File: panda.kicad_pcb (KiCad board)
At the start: 2 copper layers, 144.8 x 38.1 mm, 34 parts, among them J1 USB, J2 ICSP, U1 ATMEGA328-P, U2 MAX7219, Y1 12MHz

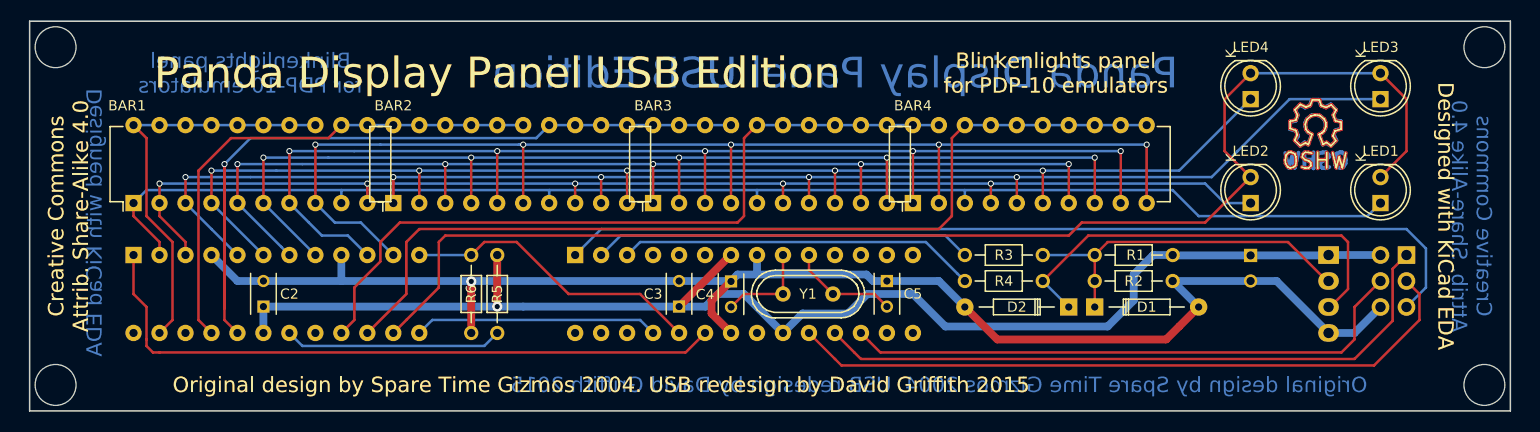
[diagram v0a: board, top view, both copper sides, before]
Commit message: Slight mods to accomodate firmware.
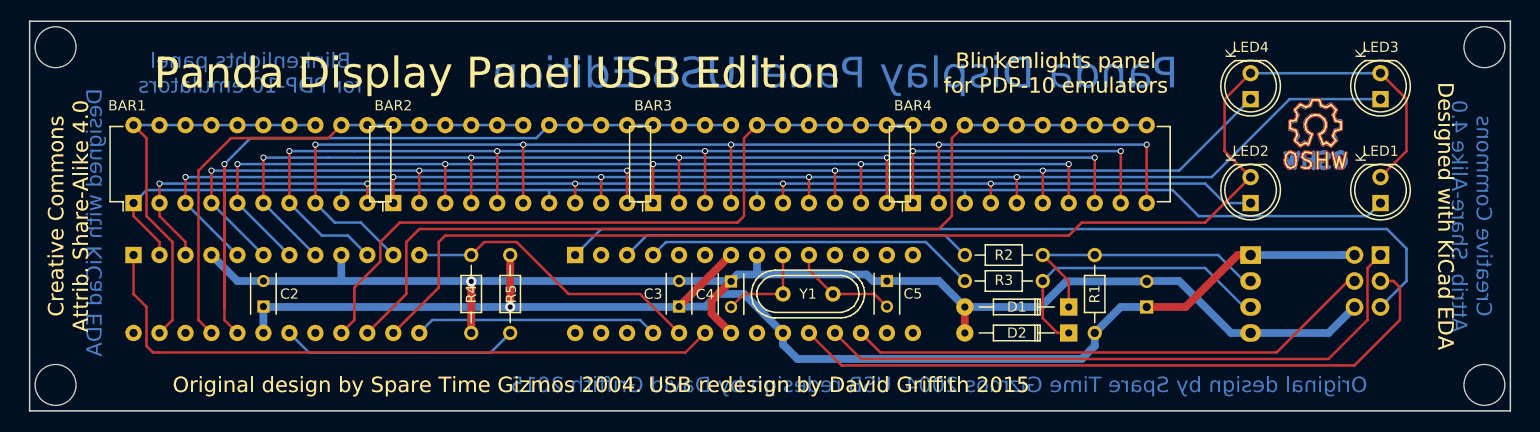
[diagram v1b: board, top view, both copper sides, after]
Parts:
- removed R6: 10K, custom_resistors:Resistor_Horizontal_RM7.62mm
- R1: value 2K2 -> 1K5; footprint custom_resistors:Resistor_Horizontal_RM7.62mm -> My_Resistors_ThroughHole:Resistor_Horizontal_RM7.62mm
- R2: value 4K7 -> 68R; footprint custom_resistors:Resistor_Horizontal_RM7.62mm -> My_Resistors_ThroughHole:Resistor_Horizontal_RM7.62mm
- R3, R5: footprint custom_resistors:Resistor_Horizontal_RM7.62mm -> My_Resistors_ThroughHole:Resistor_Horizontal_RM7.62mm
- R4: value 68R -> 10K; footprint custom_resistors:Resistor_Horizontal_RM7.62mm -> My_Resistors_ThroughHole:Resistor_Horizontal_RM7.62mm
- Y1: value 12MHz -> 16MHz
- moved R4 55.9 mm to (99.1, 109.2), turned to 270 degrees
- moved C1 11.3 mm to (165.1, 114.3), turned to 90 degrees
- moved J1 7.62 mm to (175.3, 109.2)
- moved R2 5.68 mm to (154.9, 109.2), turned to 180 degrees
- moved R3 2.54 mm to (154.9, 111.8)
- moved D2 2.54 mm to (157.5, 116.8)
- moved J2 2.54 mm to (188.0, 109.2)
- moved D1 2.54 mm to (157.5, 114.3), turned to 180 degrees
- moved R5 1.27 mm to (102.9, 116.8)
- turned R1 to 270 degrees
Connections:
- R2 pad 2: GND -> Net-(R2-Pad2)
- R3 pad 1: /D- -> /D+
- R4 pad 1: /D+ -> /LOAD
- R4 pad 2: Net-(R4-Pad2) -> GND
- U1 pad 2: Net-(R3-Pad2) -> Net-(U1-Pad2)
- U1 pad 3: Net-(R4-Pad2) -> Net-(R2-Pad2)
- U1 pad 4: Net-(U1-Pad4) -> Net-(R3-Pad2)
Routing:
- net Net-(R4-Pad2): track 35.1 -> 0.00 mm
- net Net-(R2-Pad2): track 0.00 -> 34.6 mm
- net /D+: track 42.8 -> 29.2 mm
- net GND: track 145.1 -> 137.3 mm
- net /D-: track 35.1 -> 27.5 mm
- net Net-(R3-Pad2): track 37.1 -> 32.6 mm
- net /MOSI: track 56.3 -> 51.9 mm
- net VCC: track 133.4 -> 130.3 mm
- net /MISO: track 64.1 -> 61.6 mm
- net Net-(R5-Pad1): track 21.4 -> 23.2 mm
- net /RESET: track 91.5 -> 89.9 mm
- net /SCK: track 67.2 -> 66.3 mm
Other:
- board text added: "Firmware is GPLv2. Hardware is Creative Commons 4.0 Share-Alike. See https://github.com/DavidGriffith/panda-display/ for design files and firmware."

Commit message: Update tweaks.
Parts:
- U1: value ATMEGA328-P -> ATMEGA8
- moved R5 1.27 mm to (101.6, 116.8)
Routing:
- net Net-(R5-Pad1): track 23.2 -> 21.9 mm
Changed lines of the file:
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@@
-(kicad_pcb (version 4) (host pcbnew "(2015-12-12 BZR 6370, Git 7cbf8a0)-product")
+(kicad_pcb (version 4) (host pcbnew "(2016-01-18 BZR 6495, Git cf9a9a0)-product")
   (general
     (links 130)
@@
   )
   (layers
-    (0 F.Cu signal hide)
-    (31 B.Cu signal hide)
+    (0 F.Cu signal)
+    (31 B.Cu signal)
     (32 B.Adhes user)
     (33 F.Adhes user)
@@
   )
   (setup
-    (last_trace_width 0.25)
+    (last_trace_width 0.762)
     (user_trace_width 0.5)
     (user_trace_width 0.762)
@@
       (effects (font (size 1 1) (thickness 0.15)) (justify mirror))
     )
-    (fp_text value ATMEGA328-P (at -1.905 -6.985 360) (layer B.SilkS)
+    (fp_text value ATMEGA8 (at -1.905 -4.445 360) (layer B.SilkS)
       (effects (font (size 1.5 1.5) (thickness 0.15)) (justify mirror))
     )
@@
   )
   (module My_Resistors_ThroughHole:Resistor_Horizontal_RM7.62mm (layer F.Cu)
-    (at 102.87 116.84 90)
+    (at 101.6 116.84 90)
     (descr "Resistor, Axial, RM 7.62mm, 1/4W,")
     (tags "Resistor, Axial, RM 7.62mm, 1/4W,")
@@
   (segment (start 149.86 96.52) (end 152.4 96.52) (width 0.25) (layer B.Cu) (net 13))
   (segment (start 147.32 96.52) (end 149.86 96.52) (width 0.25) (layer B.Cu) (net 13))
+  (segment (start 101.6 114.3) (end 119.34 114.3) (width 0.762) (layer B.Cu) (net 14))
+  (segment (start 119.34 114.3) (end 119.38 114.26) (width 0.762) (layer B.Cu) (net 14))
+  (segment (start 78.78 114.3) (end 101.6 114.3) (width 0.762) (layer B.Cu) (net 14))
+  (segment (start 101.6 109.22) (end 101.6 114.3) (width 0.762) (layer F.Cu) (net 14))
+  (via (at 101.6 114.3) (size 1) (drill 0.5) (layers F.Cu B.Cu) (net 14))
   (segment (start 175.26 109.22) (end 173.99 109.22) (width 0.762) (layer F.Cu) (net 14))
   (segment (start 173.99 109.22) (end 168.91 114.3) (width 0.762) (layer F.Cu) (net 14))
@@
   (segment (start 130.94863 119.38) (end 158.75 119.38) (width 0.762) (layer B.Cu) (net 14))
   (segment (start 158.75 119.38) (end 160.02 118.11) (width 0.762) (layer B.Cu) (net 14))
-  (segment (start 102.87 114.3) (end 102.87 109.22) (width 0.762) (layer F.Cu) (net 14))
-  (segment (start 102.87 114.3) (end 119.34 114.3) (width 0.762) (layer B.Cu) (net 14))
-  (segment (start 78.78 114.3) (end 102.87 114.3) (width 0.762) (layer B.Cu) (net 14))
-  (via (at 102.87 114.3) (size 1) (drill 0.5) (layers F.Cu B.Cu) (net 14))
   (segment (start 78.74 114.26) (end 78.78 114.3) (width 0.762) (layer B.Cu) (net 14))
-  (segment (start 119.34 114.3) (end 119.38 114.26) (width 0.762) (layer B.Cu) (net 14))
   (segment (start 78.74 114.26) (end 78.74 116.84) (width 0.762) (layer B.Cu) (net 14))
   (segment (start 119.38 114.26) (end 121.96 114.26) (width 0.762) (layer B.Cu) (net 14))
@@
   (segment (start 116.84 109.22) (end 118.11 107.95) (width 0.25) (layer B.Cu) (net 23))
   (segment (start 118.11 107.95) (end 143.51 107.95) (width 0.25) (layer B.Cu) (net 23))
-  (segment (start 100.965 118.745) (end 83.185 118.745) (width 0.25) (layer B.Cu) (net 24))
+  (segment (start 99.695 118.745) (end 101.6 116.84) (width 0.25) (layer B.Cu) (net 24))
+  (segment (start 99.695 118.745) (end 83.185 118.745) (width 0.25) (layer B.Cu) (net 24))
   (segment (start 83.185 118.745) (end 81.28 116.84) (width 0.25) (layer B.Cu) (net 24))
-  (segment (start 102.87 116.84) (end 100.965 118.745) (width 0.25) (layer B.Cu) (net 24))
   (segment (start 103.505 107.95) (end 100.33 107.95) (width 0.25) (layer F.Cu) (net 40))
   (segment (start 100.33 107.95) (end 99.06 109.22) (width 0.25) (layer F.Cu) (net 40))

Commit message: Final tweaks.
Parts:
- LED1, LED2, LED3, LED4: footprint MyLEDs:LED-5MM -> LEDs:LED-5MM
- moved D1 3.59 mm to (154.9, 116.8)
- moved D2 3.59 mm to (154.9, 114.3)
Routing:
- net ROW6: track 130.7 -> 144.0 mm, vias 0 -> 1
- net ROW5: track 92.1 -> 97.0 mm, vias 0 -> 1
- net ROW2: track 50.0 -> 54.4 mm, vias 0 -> 1
- net GND: track 137.3 -> 141.4 mm
- net ROW4: track 74.3 -> 78.3 mm, vias 0 -> 1
- net /D-: track 27.5 -> 31.2 mm
- net /D+: track 29.2 -> 25.6 mm
- net VCC: track 130.3 -> 130.8 mm
